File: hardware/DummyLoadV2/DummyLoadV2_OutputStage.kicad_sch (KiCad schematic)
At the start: 18 parts, among them K2 JQX-115F2Z, Q1 FQP30N06L, Q2 2N7000, U1 MAX4167, U2 MCP4725

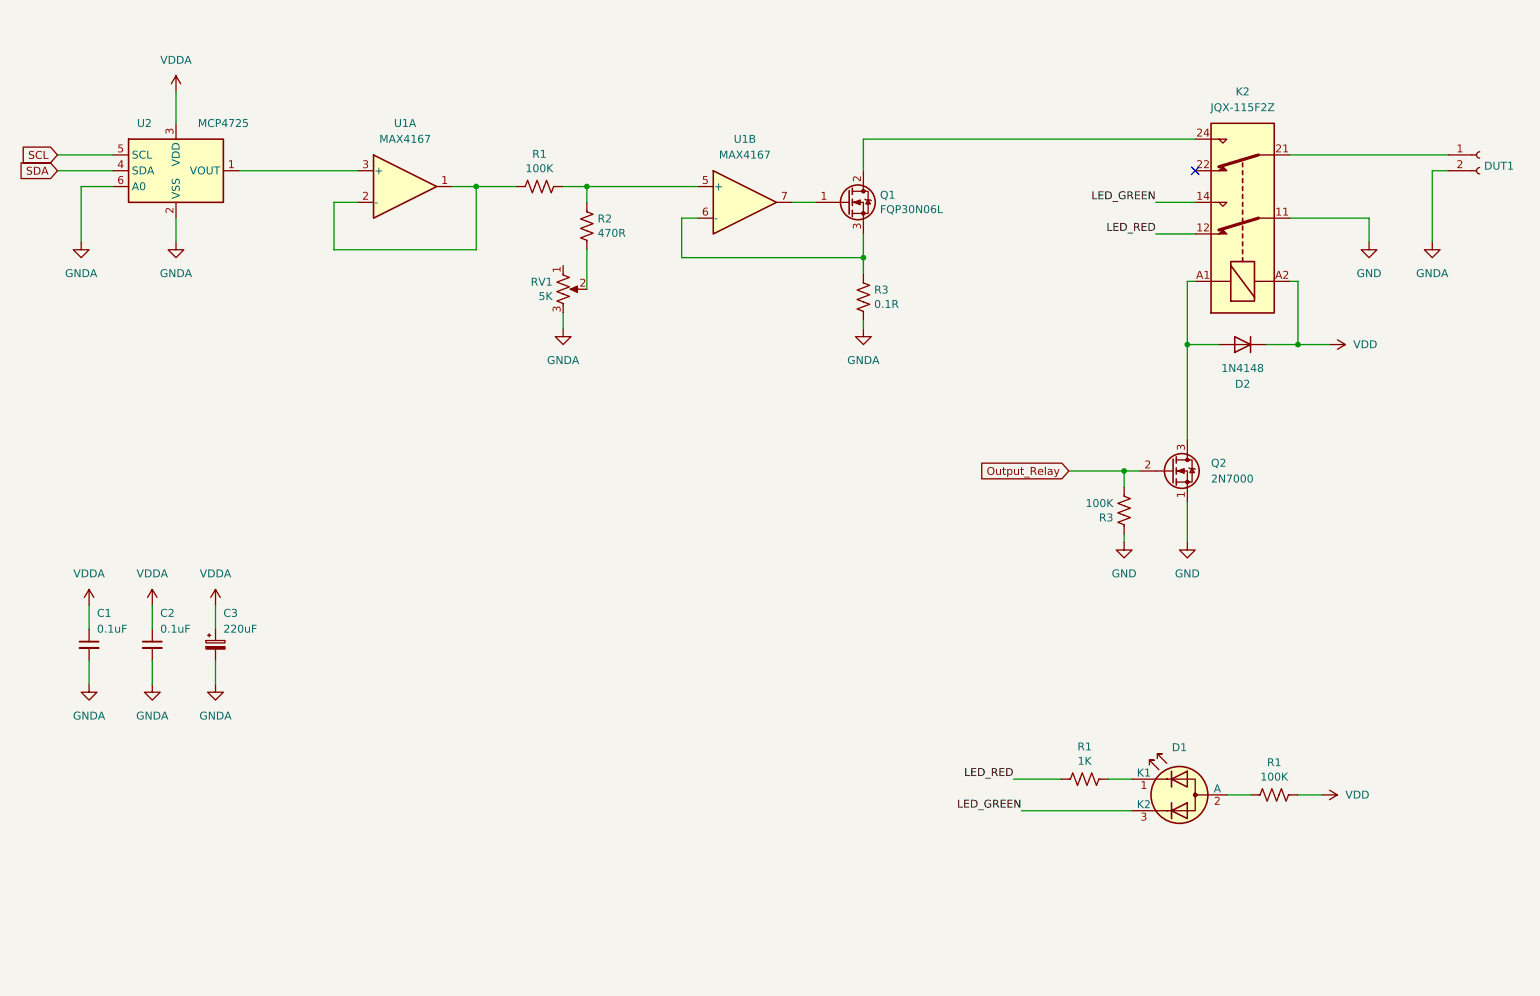
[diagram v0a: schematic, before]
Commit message: vref as variable
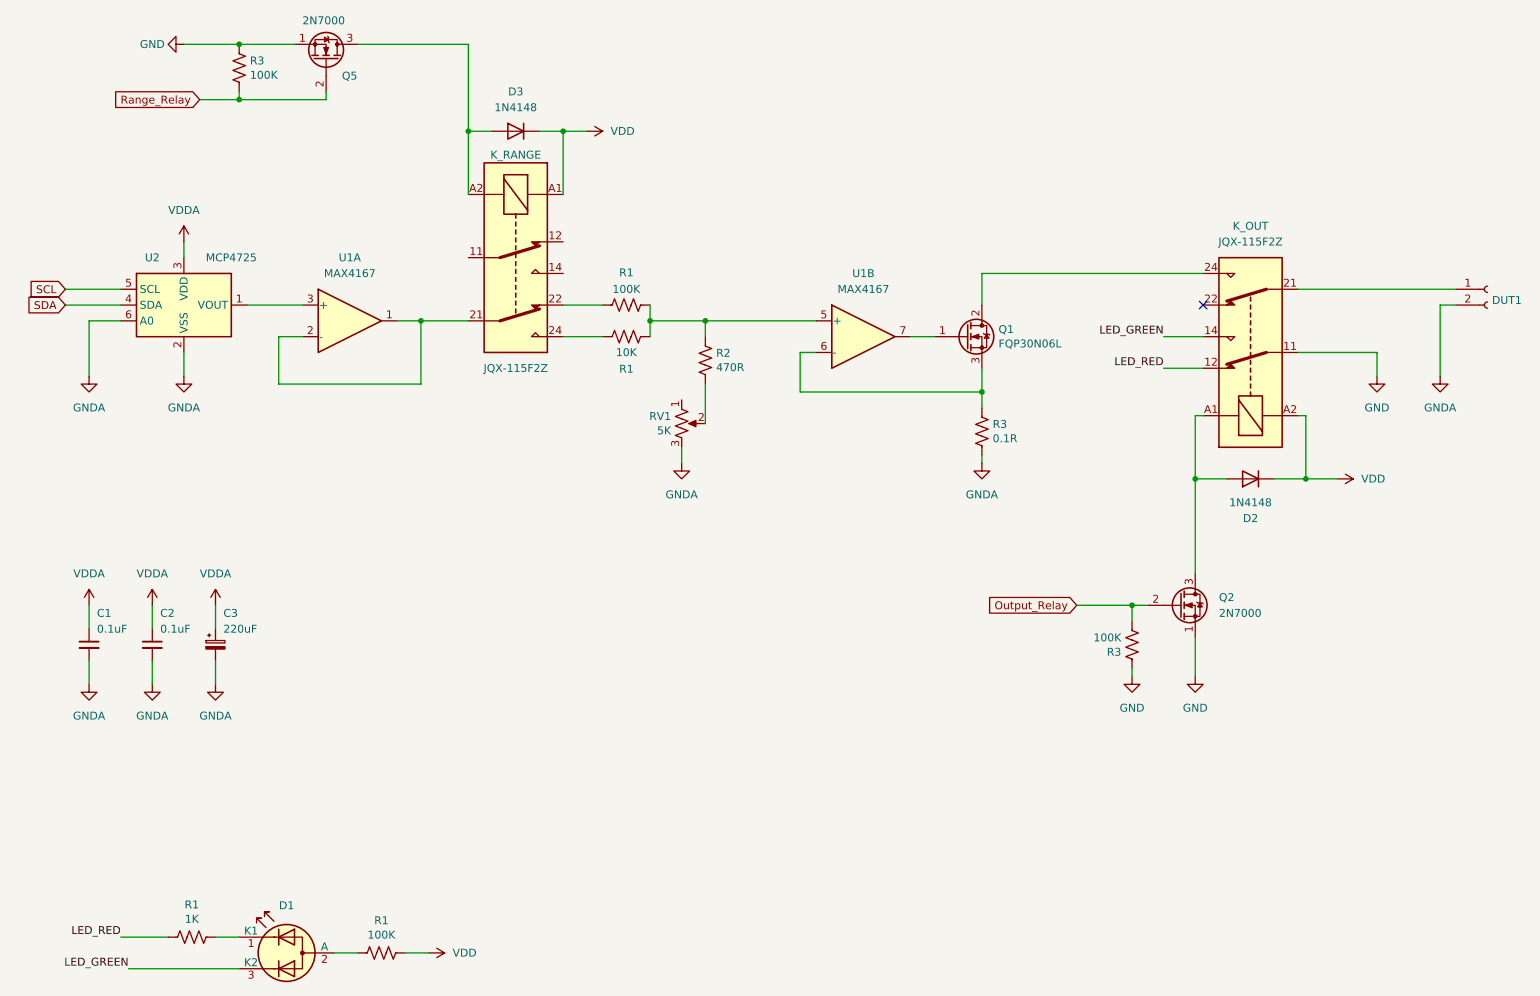
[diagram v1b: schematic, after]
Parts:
- added D3: 1N4148, Diode_THT:D_DO-35_SOD27_P7.62mm_Horizontal, symbol Diode:1N4148
- added K_RANGE: JQX-115F2Z, symbol Relay:Relay_DPDT
- added Q5: 2N7000, Package_TO_SOT_THT:TO-92_Inline, symbol Transistor_FET:2N7000
- added R1: 10K, symbol Device:R_US
- added R3: 100K, symbol Device:R_US
- renumbered K2 to K_OUT
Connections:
- net GND: now also Q5.1 (S), R3.2
- net VDD: now also D3.1 (K), K_RANGE.A1
- net at U1.1, U1.2 (-): now also K_RANGE.21; no longer R1.2
- net at R1.1, R2.2, U1.5 (+): now also R1.2
- new net: K_RANGE.24, R1.1
- new net: K_RANGE.22, R1.2
- new net: D3.2 (A), K_RANGE.A2, Q5.3 (D)
- new net Range_Relay: Q5.2 (G), R3.1
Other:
- moved on the sheet: D1, D2, DUT1, K_OUT, Q1, Q2, R1, R2, R3, RV1, U1A, U1B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

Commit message: Added hardware schematic sheets
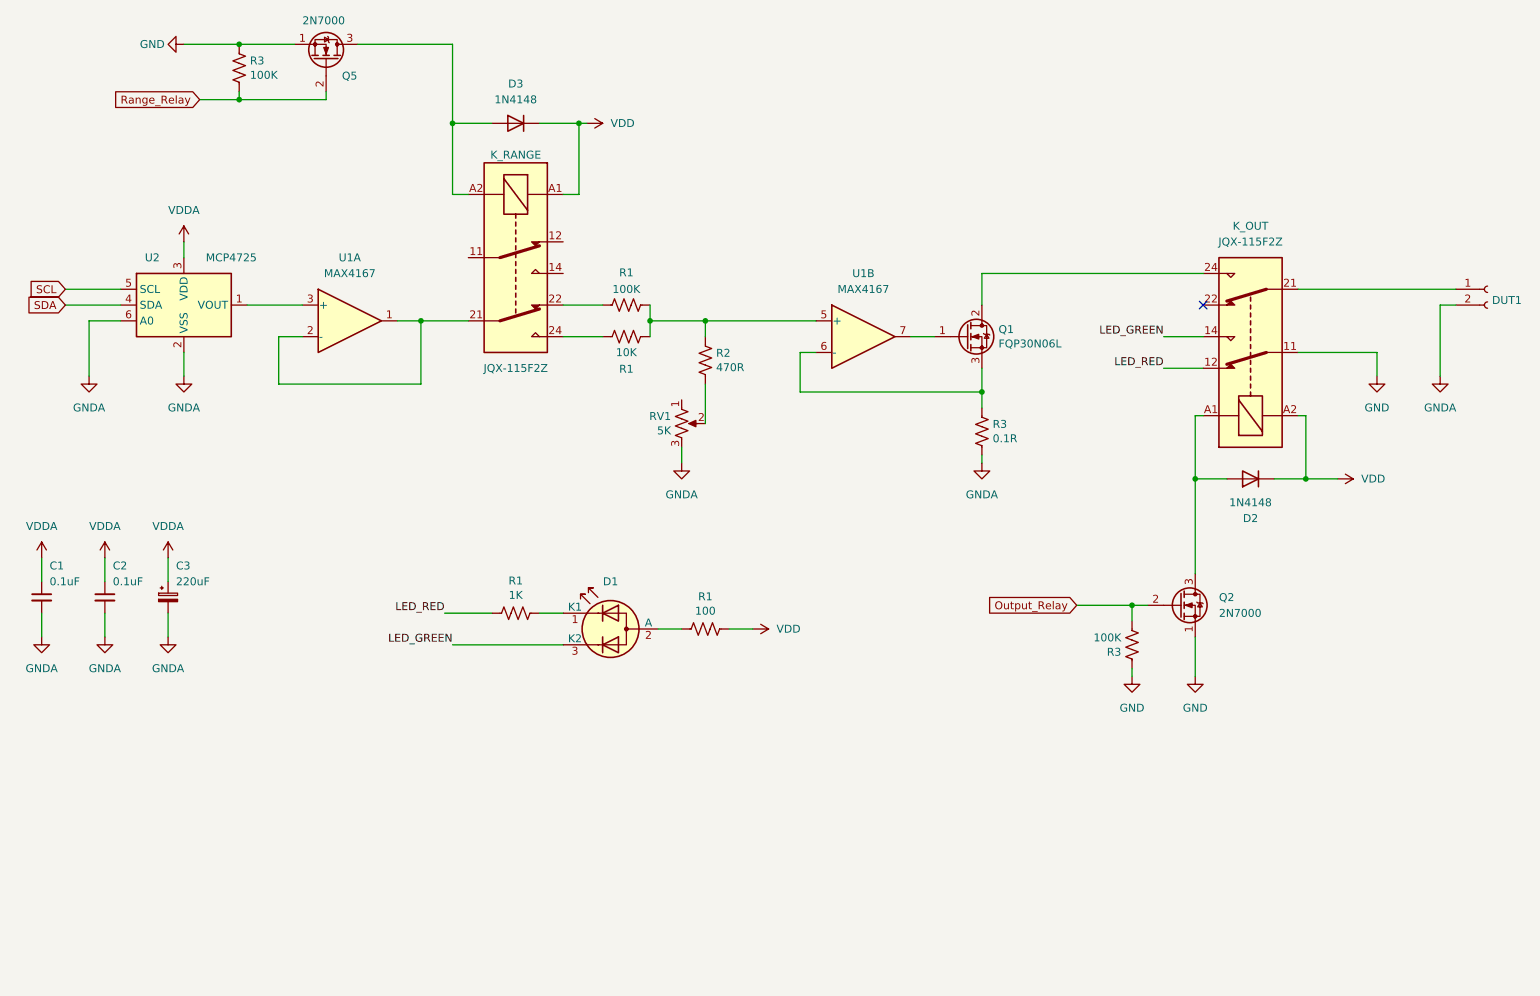
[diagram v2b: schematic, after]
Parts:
- R1: value 100K -> 100
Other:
- moved on the sheet: C1, C2, C3, D1, D3, R1
